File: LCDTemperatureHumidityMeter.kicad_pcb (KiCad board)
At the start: 2 copper layers, 94 x 71.1 mm, 11 parts, among them IC1 PIC16F1827, J1 Conn_02x01, M1 Octopus_DHT11, M2 SC1602, SW1 SW_Push

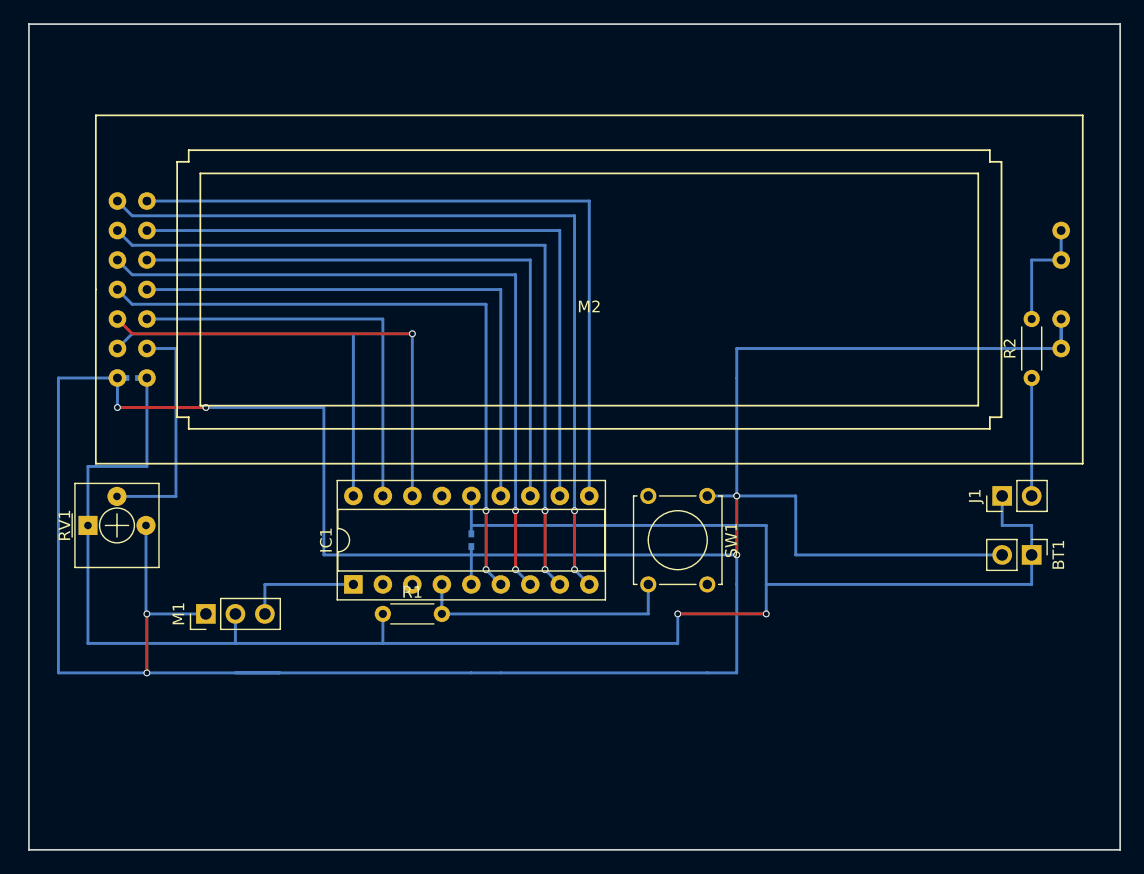
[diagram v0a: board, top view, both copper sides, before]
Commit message: 基板設計完了と，それに伴い配線の変更。
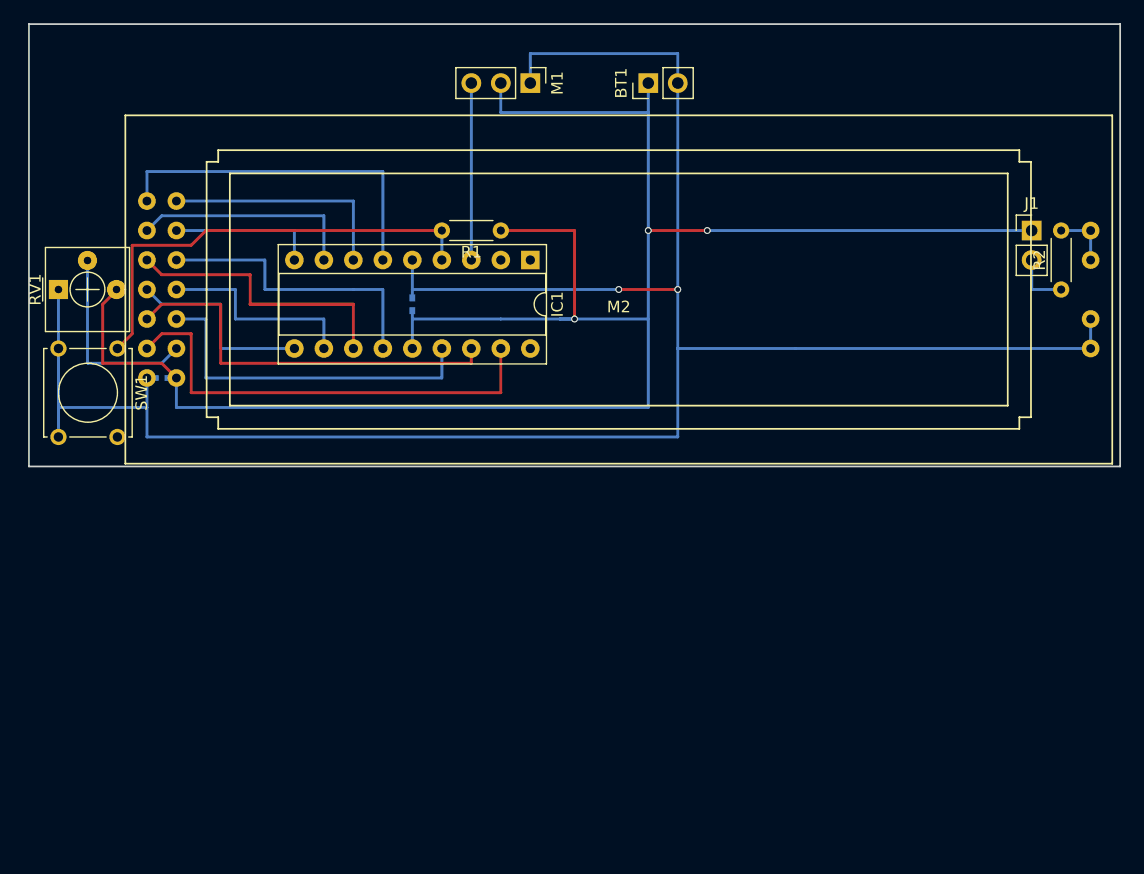
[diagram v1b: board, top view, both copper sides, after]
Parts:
- moved M1 53.6 mm to (43.2, 5.08), turned to 270 degrees
- moved SW1 52.4 mm to (7.62, 27.9)
- moved BT1 52.4 mm to (53.3, 5.08), turned to 90 degrees
- moved R1 34.5 mm to (40.6, 17.8), turned to 180 degrees
- moved IC1 31.8 mm to (43.2, 20.3), turned to 270 degrees
- moved J1 23.0 mm to (86.4, 17.8), turned to 0 degrees
- moved C1 20.9 mm to (33.0, 24.1), turned to 270 degrees
- moved RV1 20.5 mm to (2.54, 22.9)
- moved R2 8.03 mm to (88.9, 22.9)
- moved C2 2.54 mm to (11.4, 30.5)
- moved M2 2.54 mm to (50.8, 22.9)
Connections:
- M1 pad 3: Net-(IC1-Pad1) -> Net-(IC1-Pad3)
- M2 pad 10: Net-(IC1-Pad7) -> Net-(IC1-Pad12)
- M2 pad 11: Net-(IC1-Pad11) -> Net-(IC1-Pad9)
- M2 pad 13: Net-(IC1-Pad10) -> Net-(IC1-Pad7)
- M2 pad 14: Net-(IC1-Pad9) -> Net-(IC1-Pad6)
- M2 pad 4: Net-(IC1-Pad18) -> Net-(IC1-Pad17)
- M2 pad 5: Net-(IC1-Pad17) -> Net-(IC1-Pad15)
- M2 pad 7: Net-(IC1-Pad13) -> Net-(IC1-Pad11)
- M2 pad 8: Net-(IC1-Pad6) -> Net-(IC1-Pad10)
- M2 pad 9: Net-(IC1-Pad12) -> Net-(IC1-Pad13)
- RV1 pad 1: VCC -> GND
- RV1 pad 3: GND -> VCC
- SW1 pad 1: GND -> Net-(IC1-Pad4)
- SW1 pad 2: Net-(IC1-Pad4) -> GND
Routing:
- net GND: track 274.5 -> 191.9 mm, vias 6 -> 2
- net Net-(IC1-Pad9): track 72.2 -> 12.7 mm, vias 2 -> 0
- net Net-(IC1-Pad8): track 67.1 -> 19.6 mm, vias 2 -> 0
- net Net-(IC1-Pad10): track 63.5 -> 17.0 mm
- net Net-(IC1-Pad7): track 62.0 -> 20.3 mm, vias 2 -> 0
- net Net-(IC1-Pad11): track 58.4 -> 17.8 mm
- net Net-(IC1-Pad18): track 34.8 -> 0.00 mm
- net Net-(IC1-Pad15): track 0.00 -> 30.5 mm
- net Net-(IC1-Pad6): track 56.9 -> 30.5 mm, vias 2 -> 0
- net Net-(IC1-Pad13): track 48.3 -> 25.4 mm
- net Net-(IC1-Pad12): track 53.3 -> 33.5 mm
- net Net-(IC1-Pad4): track 22.9 -> 39.3 mm
- net Net-(IC1-Pad3): track 0.00 -> 15.2 mm
- net Net-(IC1-Pad1): track 10.2 -> 0.00 mm
- net VCC: track 164.0 -> 172.6 mm, vias 2 -> 3
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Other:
- board size 94 x 71.1 mm -> 94 x 38.1 mm
